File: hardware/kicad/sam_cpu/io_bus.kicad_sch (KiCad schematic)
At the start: 19 parts, among them J9 J9 IO BUS, Q3 2N7002, U6 SN74LVC8T245, U7 74AHCT541

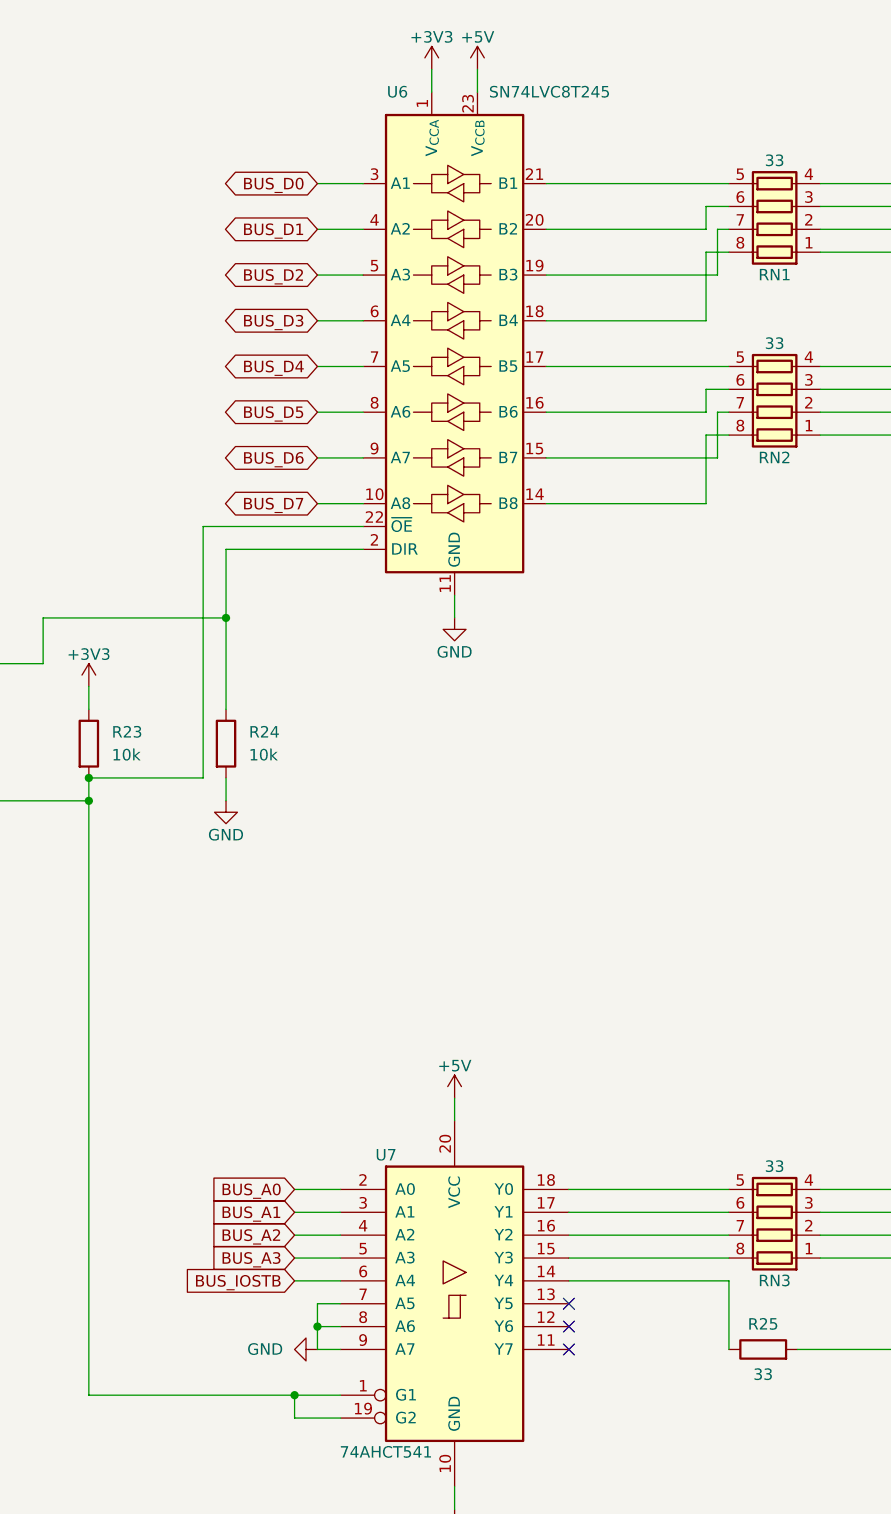
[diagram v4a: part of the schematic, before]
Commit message: RP2354B fan-out: turn the bus buffers, fix the USB pair, RS485 resistors at U4
- IO bus sheet: U6 / U7 channel order reversed (bit order on U4 and J9 unchanged).
- Board: U6 / U7 turned 180 degrees in place so their RP2354B side faces U4;
  R13 / R14 swapped so USB D+/D- leave U4 without crossing; R205 / R207 / R209
  moved next to U4. Bus, USB and RS485 nets ripped for re-routing.
- Change scripts c21 / c22; ERC 0, schematic parity 0.

Co-Authored-By: Claude Opus 5.5 (1M context) <noreply@anthropic.com>
Claude-Session: https://claude.ai/code/session_01ExuDVoDDDHhVWjb8EwVzYb
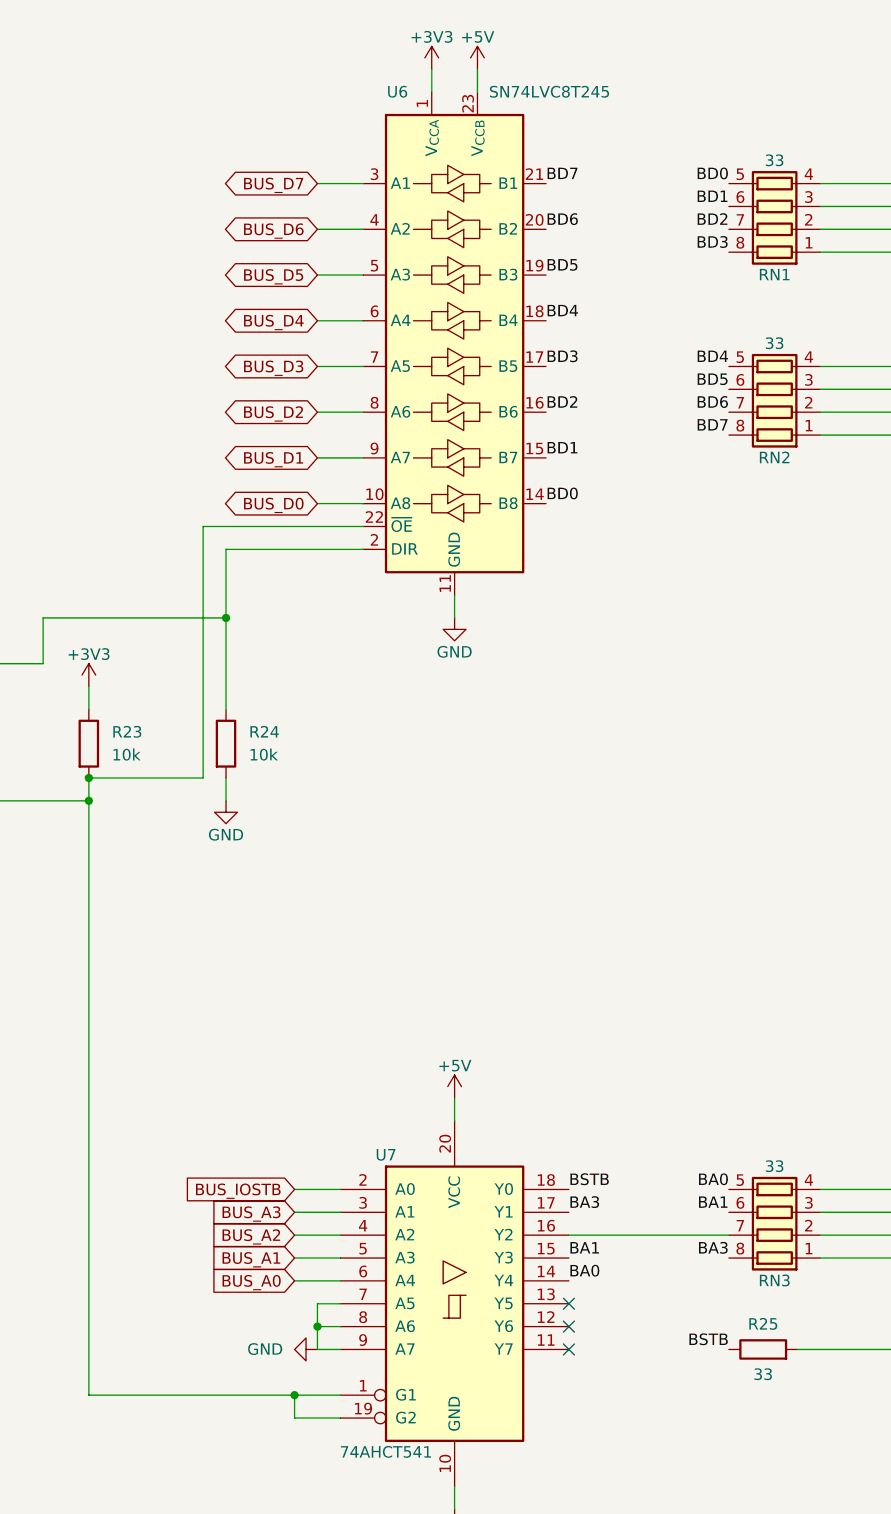
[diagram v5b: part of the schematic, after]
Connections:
- net BUS_A0: now also U7.6 (A4); no longer U7.2 (A0)
- net BUS_A1: now also U7.5 (A3); no longer U7.3 (A1)
- net BUS_A3: now also U7.3 (A1); no longer U7.5 (A3)
- net BUS_D0: now also U6.10 (A8); no longer U6.3 (A1)
- net BUS_D1: now also U6.9 (A7); no longer U6.4 (A2)
- net BUS_D2: now also U6.8 (A6); no longer U6.5 (A3)
- net BUS_D3: now also U6.7 (A5); no longer U6.6 (A4)
- net BUS_D4: now also U6.6 (A4); no longer U6.7 (A5)
- net BUS_D5: now also U6.5 (A3); no longer U6.8 (A6)
- net BUS_D6: now also U6.4 (A2); no longer U6.9 (A7)
- net BUS_D7: now also U6.3 (A1); no longer U6.10 (A8)
- net BUS_IOSTB: now also U7.2 (A0); no longer U7.6 (A4)
- net BD0: now reaches U6.14 (B8)
- net BD0: now also RN1.5 (R4.2); no longer RN2.8 (R1.2)
- net BD1: now reaches U6.15 (B7)
- net BD1: now also RN1.6 (R3.2); no longer RN2.7 (R2.2)
- net BD2: now reaches U6.16 (B6)
- net BD2: now also RN1.7 (R2.2); no longer RN2.6 (R3.2)
- net BD3: now reaches U6.17 (B5)
- net BD3: now also RN1.8 (R1.2); no longer RN2.5 (R4.2)
- net BD4: now reaches U6.18 (B4)
- net BD4: now also RN2.5 (R4.2); no longer RN1.8 (R1.2)
- net BD5: now reaches U6.19 (B3)
- net BD5: now also RN2.6 (R3.2); no longer RN1.7 (R2.2)
- net BD6: now reaches U6.20 (B2)
- net BD6: now also RN2.7 (R2.2); no longer RN1.6 (R3.2)
- net BD7: now reaches U6.21 (B1)
- net BD7: now also RN2.8 (R1.2); no longer RN1.5 (R4.2)
- net BA0: now reaches U7.14 (Y4)
- net BA0: now also RN3.5 (R4.2); no longer R25.1
- net BA1: now reaches U7.15 (Y3)
- net BA1: now also RN3.6 (R3.2); no longer RN3.8 (R1.2)
- net BA3: now reaches U7.17 (Y1)
- net BA3: now also RN3.8 (R1.2); no longer RN3.6 (R3.2)
- net BSTB: now reaches U7.18 (Y0)
- net BSTB: now also R25.1; no longer RN3.5 (R4.2)

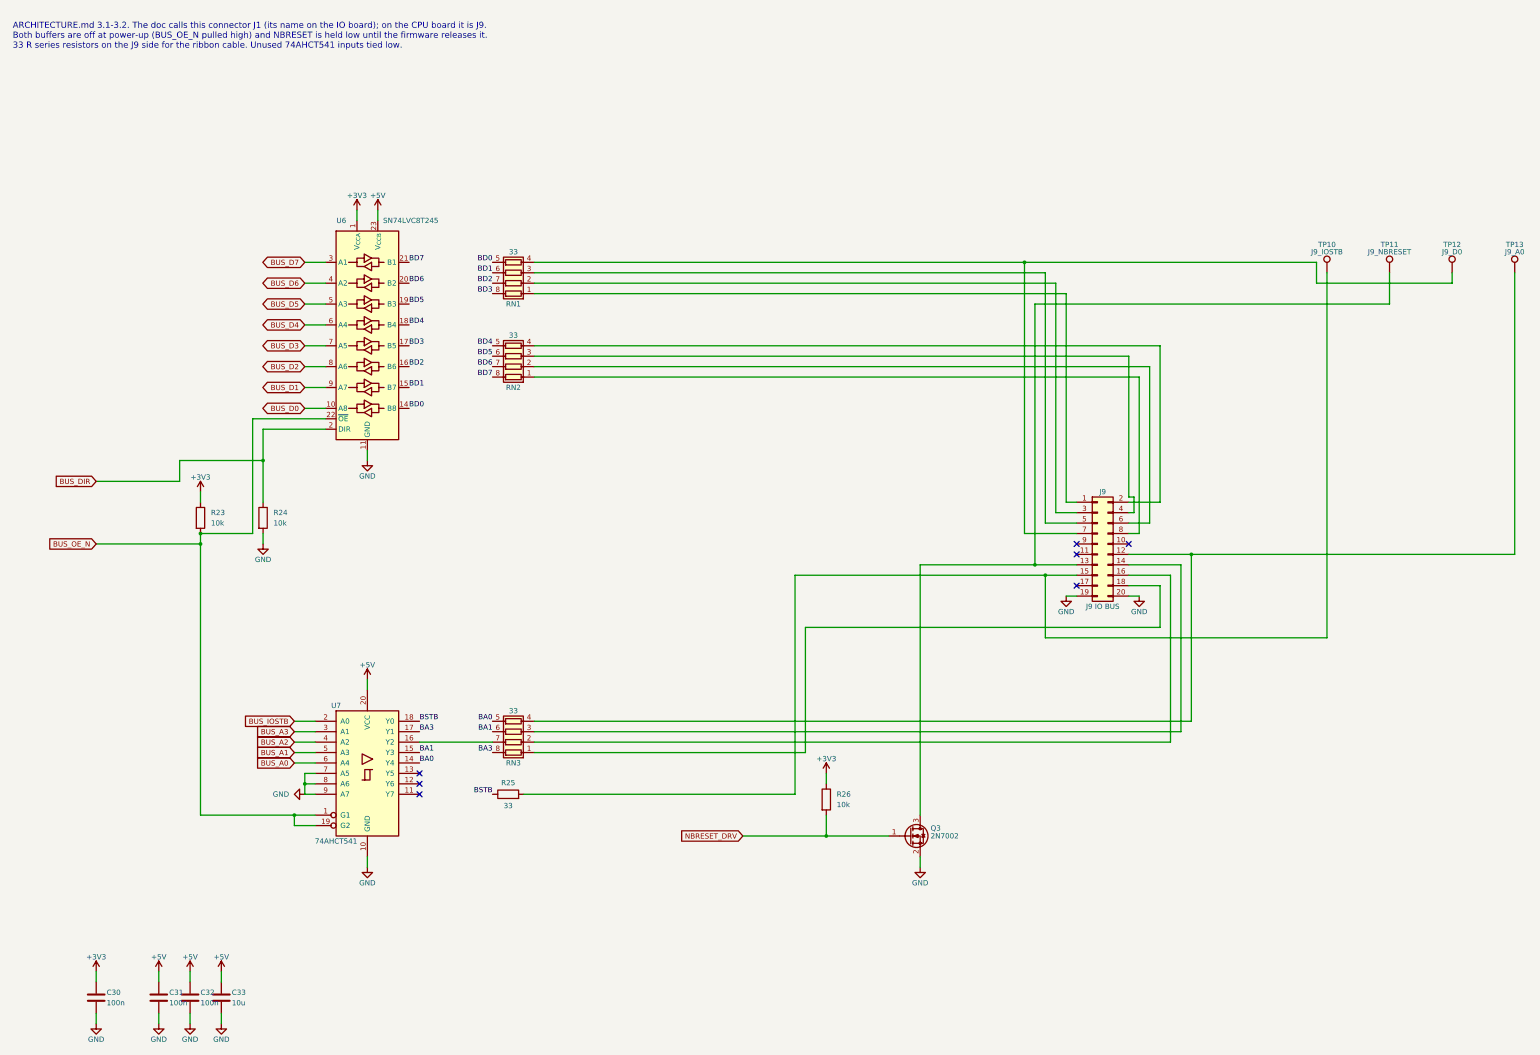
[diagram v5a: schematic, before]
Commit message: DIP switch block not loaded; larger schematic text
c30: SW3, R168-R175, U14 and C93 flagged DNP (schematic and board).
c31: schematic text 1.27 -> 1.6 mm (pins 1.5 mm), intersheet refs moved out.

Co-Authored-By: Claude Opus 5.5 (1M context) <noreply@anthropic.com>
Claude-Session: https://claude.ai/code/session_01ExuDVoDDDHhVWjb8EwVzYb
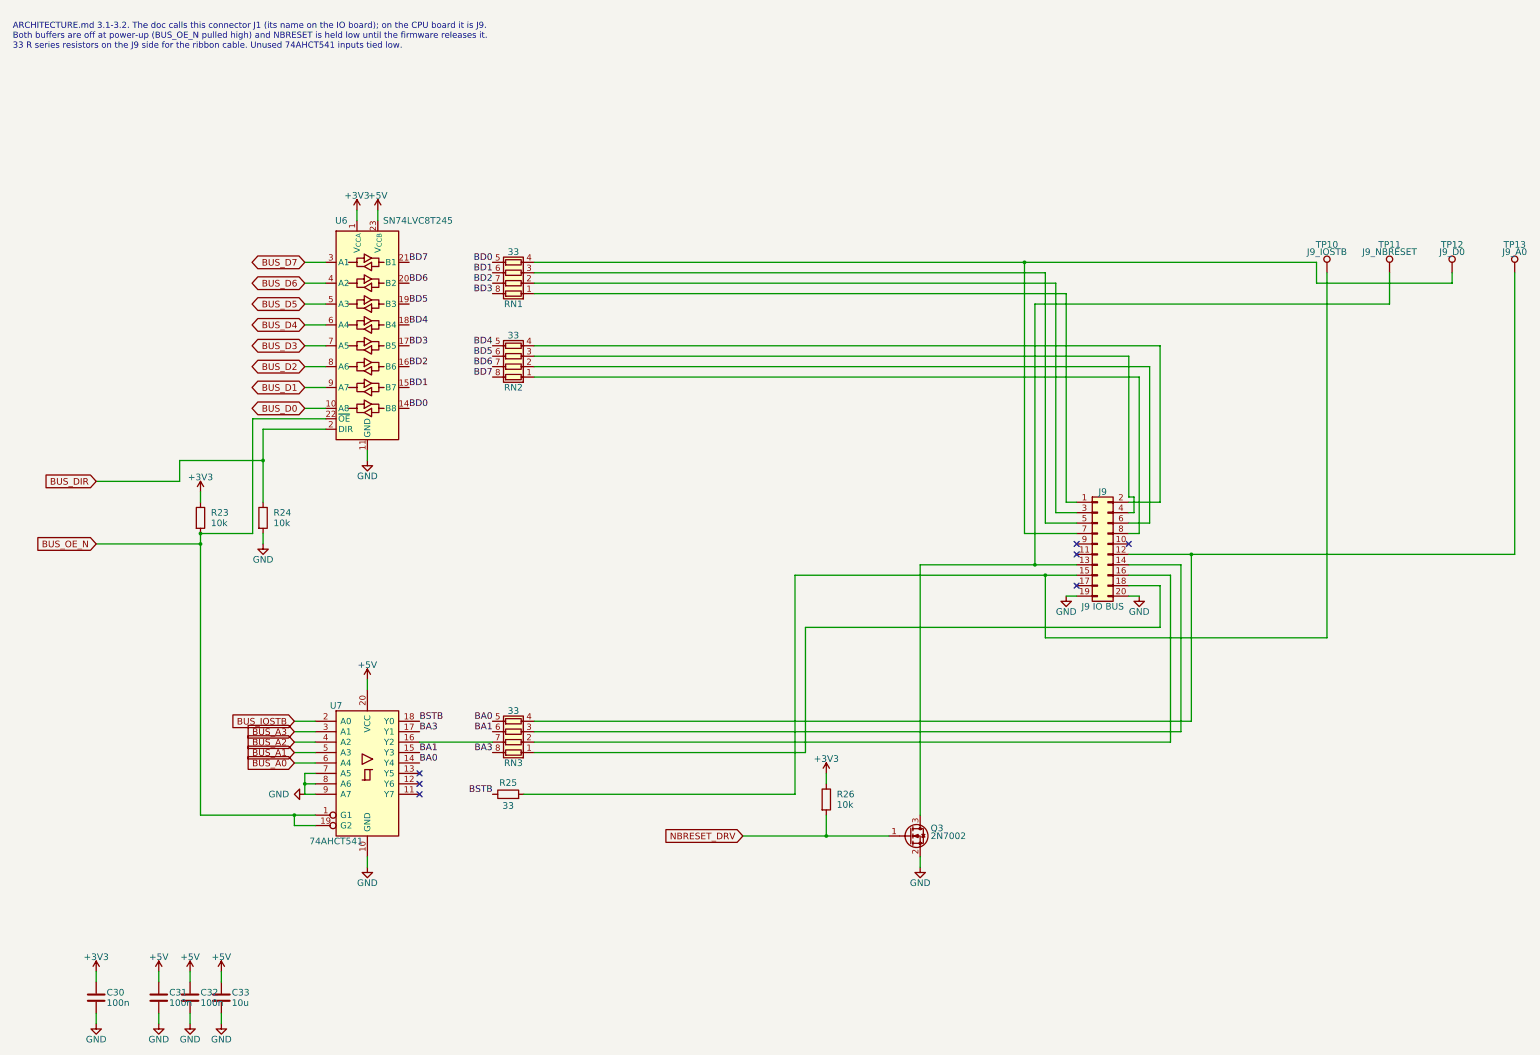
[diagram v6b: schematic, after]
